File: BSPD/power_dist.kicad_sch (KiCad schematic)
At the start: 6 parts, among them U6 LM7805_TO220, U8 LM7809_TO220

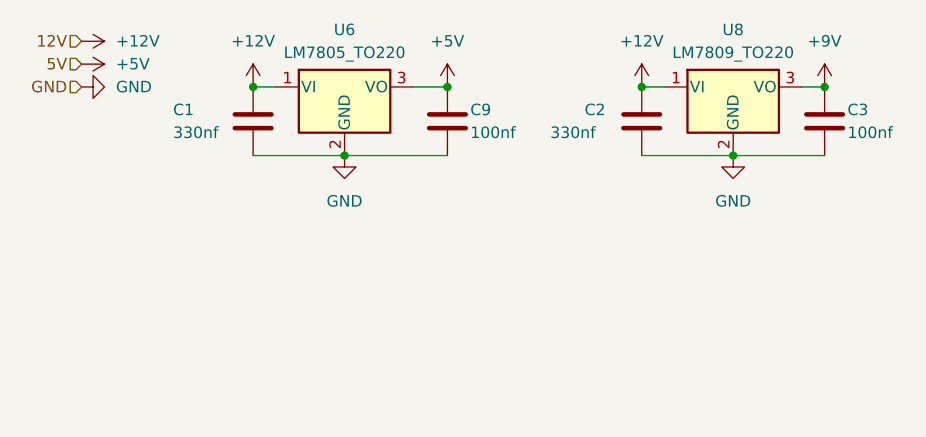
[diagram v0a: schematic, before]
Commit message: Overhaul of BPSD to V3.0
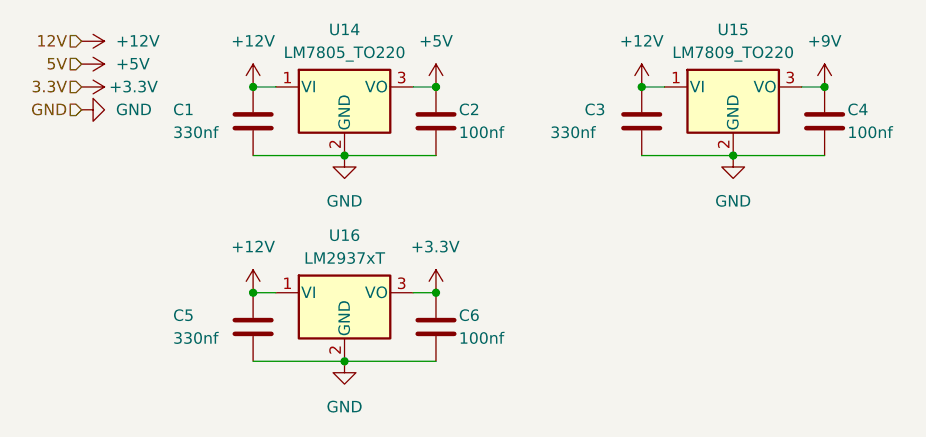
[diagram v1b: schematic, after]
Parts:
- added C5: 330nf, Capacitor_SMD:C_0805_2012Metric_Pad1.18x1.45mm_HandSolder, symbol Device:C
- added C6: 100nf, Capacitor_SMD:C_0805_2012Metric_Pad1.18x1.45mm_HandSolder, symbol Device:C
- added U16: LM2937xT, Package_TO_SOT_THT:TO-220-3_Vertical, symbol Regulator_Linear:LM2937xT
- renumbered C9 to C2, C2 to C3, C3 to C4, U6 to U14, U8 to U15
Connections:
- net +12V: now also C5.1, U16.1 (VI)
- net GND: now also C5.2, C6.2, U16.2 (GND)
- new net +3.3V: C6.1, U16.3 (VO)
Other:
- moved on the sheet: C2

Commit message: Added brake sensor power and ground on schem and pcb
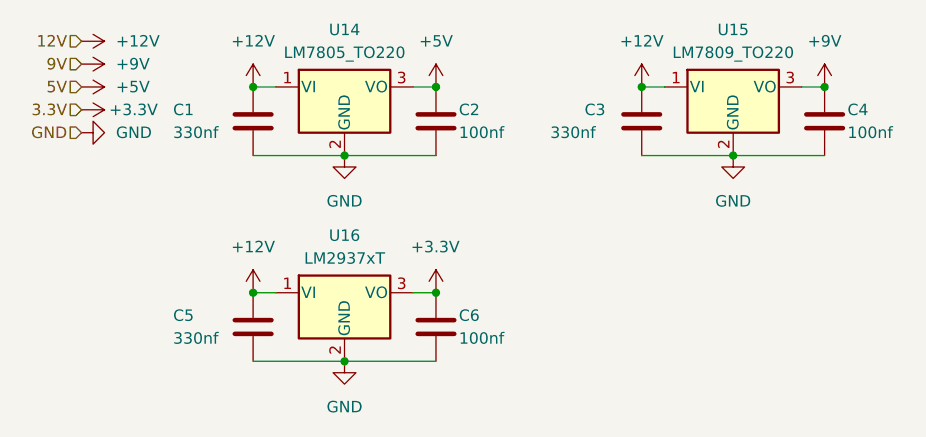
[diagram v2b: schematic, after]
